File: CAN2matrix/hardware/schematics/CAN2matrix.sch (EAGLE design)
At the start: 31 parts, among them IC1 MEGA8-P, IC2 MCP2515-E/P, IC3 MCP2515-E/P, U1 MCP2551P, U2 MCP2551P, X1 CAN1, X2 CAN2

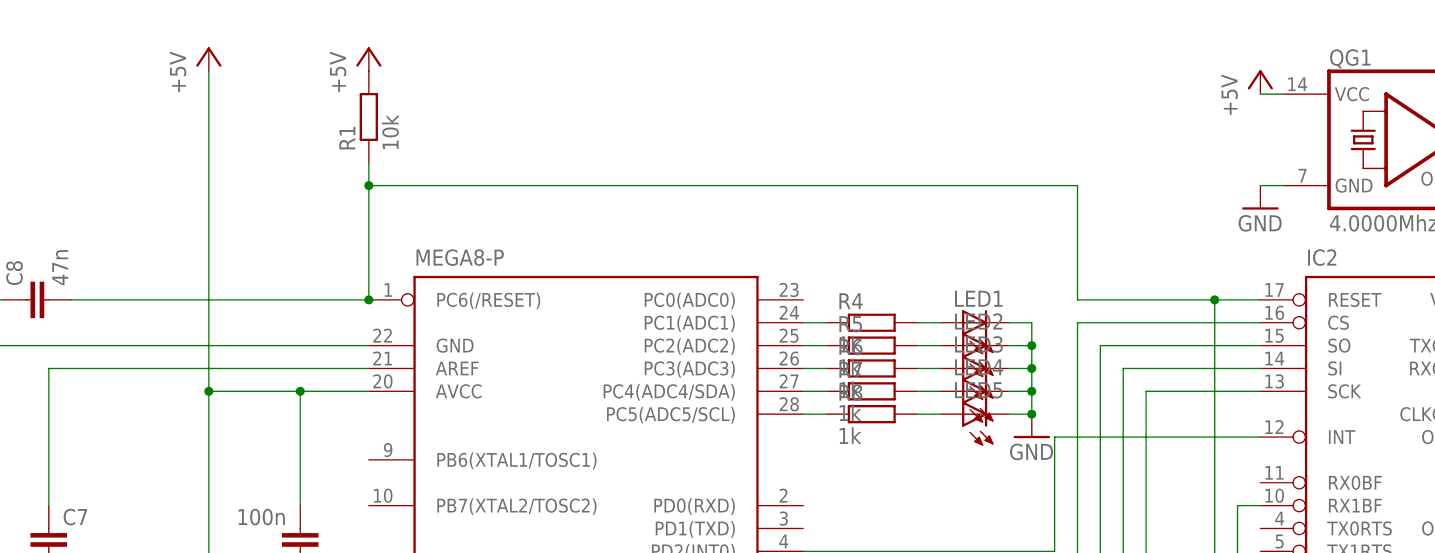
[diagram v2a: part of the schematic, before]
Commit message: add light dependent resistor for dimming; update schematics and image
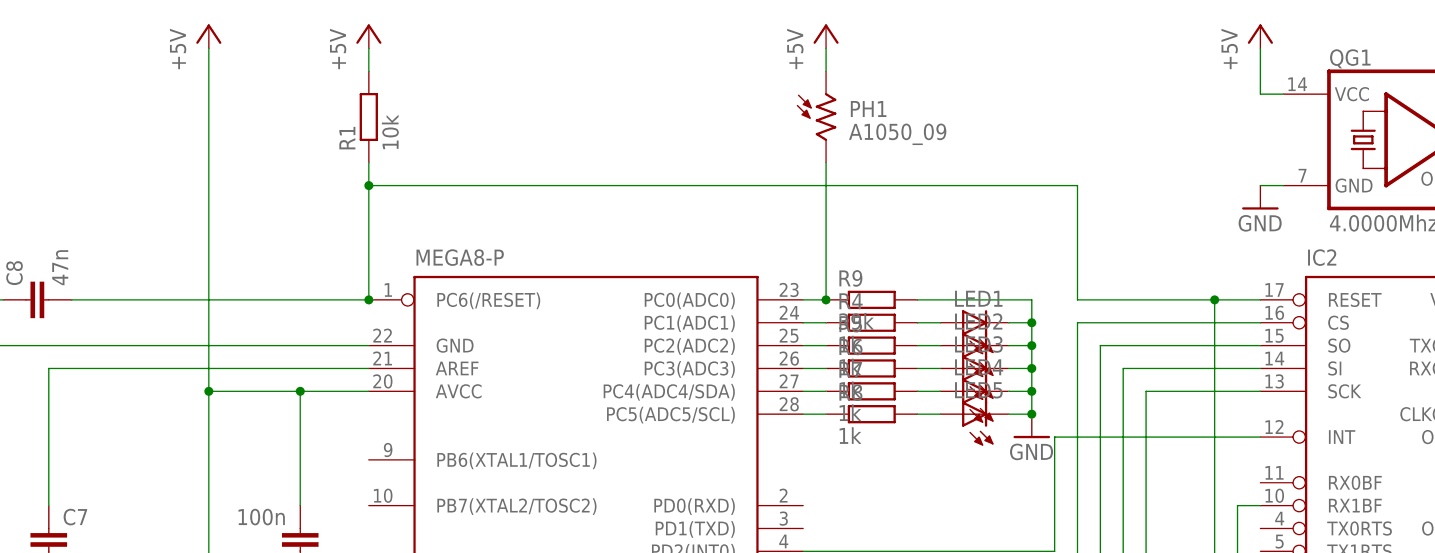
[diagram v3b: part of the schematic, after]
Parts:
- added PH1: A1050_09, photo-elements:A1050_09
- added R9: 39k, resistor:R-EU_0207/2V
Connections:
- new net N$32: IC1.PC0(ADC0), PH1.2, R9.1
- net +5V: now also PH1.1
- net GND: now also R9.2
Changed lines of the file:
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@@
 <grid distance="0.1" unitdist="inch" unit="inch" style="lines" multiple="1" display="no" altdistance="0.01" altunitdist="inch" altunit="inch"/>
 <layers>
-<layer number="1" name="Top" color="4" fill="1" visible="yes" active="no"/>
-<layer number="16" name="Bottom" color="1" fill="1" visible="yes" active="no"/>
-<layer number="17" name="Pads" color="2" fill="1" visible="yes" active="no"/>
-<layer number="18" name="Vias" color="2" fill="1" visible="yes" active="no"/>
-<layer number="19" name="Unrouted" color="6" fill="1" visible="yes" active="no"/>
-<layer number="20" name="Dimension" color="15" fill="1" visible="yes" active="no"/>
-<layer number="21" name="tPlace" color="7" fill="1" visible="yes" active="no"/>
-<layer number="22" name="bPlace" color="7" fill="1" visible="yes" active="no"/>
-<layer number="23" name="tOrigins" color="15" fill="1" visible="yes" active="no"/>
-<layer number="24" name="bOrigins" color="15" fill="1" visible="yes" active="no"/>
-<layer number="25" name="tNames" color="7" fill="1" visible="yes" active="no"/>
-<layer number="26" name="bNames" color="7" fill="1" visible="yes" active="no"/>
-<layer number="27" name="tValues" color="7" fill="1" visible="yes" active="no"/>
-<layer number="28" name="bValues" color="7" fill="1" visible="yes" active="no"/>
+<layer number="1" name="Top" color="4" fill="1" visible="no" active="no"/>
+<layer number="16" name="Bottom" color="1" fill="1" visible="no" active="no"/>
+<layer number="17" name="Pads" color="2" fill="1" visible="no" active="no"/>
+<layer number="18" name="Vias" color="2" fill="1" visible="no" active="no"/>
+<layer number="19" name="Unrouted" color="6" fill="1" visible="no" active="no"/>
+<layer number="20" name="Dimension" color="15" fill="1" visible="no" active="no"/>
+<layer number="21" name="tPlace" color="7" fill="1" visible="no" active="no"/>
+<layer number="22" name="bPlace" color="7" fill="1" visible="no" active="no"/>
+<layer number="23" name="tOrigins" color="15" fill="1" visible="no" active="no"/>
+<layer number="24" name="bOrigins" color="15" fill="1" visible="no" active="no"/>
+<layer number="25" name="tNames" color="7" fill="1" visible="no" active="no"/>
+<layer number="26" name="bNames" color="7" fill="1" visible="no" active="no"/>
+<layer number="27" name="tValues" color="7" fill="1" visible="no" active="no"/>
+<layer number="28" name="bValues" color="7" fill="1" visible="no" active="no"/>
 <layer number="29" name="tStop" color="7" fill="3" visible="no" active="no"/>
 <layer number="30" name="bStop" color="7" fill="6" visible="no" active="no"/>
@@
 <layer number="35" name="tGlue" color="7" fill="4" visible="no" active="no"/>
 <layer number="36" name="bGlue" color="7" fill="5" visible="no" active="no"/>
-<layer number="37" name="tTest" color="7" fill="1" visible="yes" active="no"/>
-<layer number="38" name="bTest" color="7" fill="1" visible="yes" active="no"/>
+<layer number="37" name="tTest" color="7" fill="1" visible="no" active="no"/>
+<layer number="38" name="bTest" color="7" fill="1" visible="no" active="no"/>
 <layer number="39" name="tKeepout" color="4" fill="11" visible="no" active="no"/>
 <layer number="40" name="bKeepout" color="1" fill="11" visible="no" active="no"/>
@@
 <layer number="44" name="Drills" color="7" fill="1" visible="no" active="no"/>
 <layer number="45" name="Holes" color="7" fill="1" visible="no" active="no"/>
-<layer number="46" name="Milling" color="3" fill="1" visible="yes" active="no"/>
-<layer number="47" name="Measures" color="7" fill="1" visible="yes" active="no"/>
-<layer number="48" name="Document" color="7" fill="1" visible="yes" active="no"/>
-<layer number="49" name="Reference" color="7" fill="1" visible="yes" active="no"/>
-<layer number="51" name="tDocu" color="6" fill="9" visible="yes" active="no"/>
-<layer number="52" name="bDocu" color="7" fill="1" visible="yes" active="no"/>
+<layer number="46" name="Milling" color="3" fill="1" visible="no" active="no"/>
+<layer number="47" name="Measures" color="7" fill="1" visible="no" active="no"/>
+<layer number="48" name="Document" color="7" fill="1" visible="no" active="no"/>
+<layer number="49" name="Reference" color="7" fill="1" visible="no" active="no"/>
+<layer number="51" name="tDocu" color="6" fill="9" visible="no" active="no"/>
+<layer number="52" name="bDocu" color="7" fill="1" visible="no" active="no"/>
 <layer number="91" name="Nets" color="2" fill="1" visible="yes" active="yes"/>
 <layer number="92" name="Busses" color="1" fill="1" visible="yes" active="yes"/>
@@
 <part name="LED5" library="led" deviceset="LED" device="3MM"/>
 <part name="GND11" library="supply1" deviceset="GND" device=""/>
+<part name="R9" library="resistor" deviceset="R-EU_" device="0207/2V" value="39k"/>
+<part name="PH1" library="photo-elements" deviceset="A10" device="" technology="50_09"/>
+<part name="P+5" library="supply1" deviceset="+5V" device=""/>
 </parts>
 <sheets>
@@
 <instance part="R2" gate="G$1" x="111.76" y="25.4" rot="R90"/>
 <instance part="R3" gate="G$1" x="111.76" y="-40.64" rot="R90"/>
-<instance part="P+1" gate="1" x="-78.74" y="66.04"/>
+<instance part="P+1" gate="1" x="-78.74" y="68.58"/>
 <instance part="GND1" gate="1" x="-144.78" y="-81.28"/>
-<instance part="P+2" gate="1" x="-96.52" y="66.04"/>
+<instance part="P+2" gate="1" x="-96.52" y="68.58"/>
 <instance part="P+3" gate="1" x="53.34" y="48.26"/>
 <instance part="P+4" gate="1" x="50.8" y="-17.78"/>
@@
 <instance part="C8" gate="G$1" x="-116.84" y="38.1" rot="R90"/>
 <instance part="QG1" gate="G$1" x="35.56" y="55.88"/>
-<instance part="P+10" gate="1" x="20.32" y="63.5"/>
+<instance part="P+10" gate="1" x="20.32" y="68.58"/>
 <instance part="GND8" gate="1" x="20.32" y="48.26"/>
 <instance part="SV1" gate="G$1" x="-17.78" y="-68.58" rot="R180"/>
@@
 <instance part="LED5" gate="G$1" x="-12.7" y="25.4" rot="R90"/>
 <instance part="GND11" gate="1" x="-5.08" y="22.86"/>
+<instance part="R9" gate="G$1" x="-22.86" y="38.1"/>
+<instance part="PH1" gate="G$1" x="-27.94" y="58.42"/>
+<instance part="P+5" gate="1" x="-27.94" y="68.58"/>
 </instances>
 <busses>
@@
 <pinref part="R1" gate="G$1" pin="2"/>
 <pinref part="P+1" gate="1" pin="+5V"/>
+<wire x1="-78.74" y1="66.04" x2="-78.74" y2="63.5" width="0.1524" layer="91"/>
 </segment>
 <segment>
@@
 <segment>
 <pinref part="P+2" gate="1" pin="+5V"/>
-<wire x1="-96.52" y1="63.5" x2="-96.52" y2="27.94" width="0.1524" layer="91"/>
+<wire x1="-96.52" y1="66.04" x2="-96.52" y2="27.94" width="0.1524" layer="91"/>
 <pinref part="IC1" gate="G$1" pin="VCC@1"/>
 <wire x1="-96.52" y1="27.94" x2="-96.52" y2="2.54" width="0.1524" layer="91"/>
@@
 </segment>
 <segment>
-<pinref part="QG1" gate="G$1" pin="VCC"/>
-<pinref part="P+10" gate="1" pin="+5V"/>
-<wire x1="20.32" y1="60.96" x2="22.86" y2="60.96" width="0.1524" layer="91"/>
-</segment>
-<segment>
 <pinref part="IC2" gate="G$1" pin="VDD"/>
 <pinref part="P+3" gate="1" pin="+5V"/>
@@
 <pinref part="SV2" gate="G$1" pin="1"/>
 <wire x1="-10.16" y1="-50.8" x2="-7.62" y2="-50.8" width="0.1524" layer="91"/>
+</segment>
+<segment>
+<pinref part="P+10" gate="1" pin="+5V"/>
+<wire x1="20.32" y1="66.04" x2="20.32" y2="60.96" width="0.1524" layer="91"/>
+<pinref part="QG1" gate="G$1" pin="VCC"/>
+<wire x1="20.32" y1="60.96" x2="22.86" y2="60.96" width="0.1524" layer="91"/>
+</segment>
+<segment>
+<pinref part="P+5" gate="1" pin="+5V"/>
+<pinref part="PH1" gate="G$1" pin="1"/>
+<wire x1="-27.94" y1="66.04" x2="-27.94" y2="63.5" width="0.1524" layer="91"/>
 </segment>
 </net>
@@
 <junction x="-5.08" y="27.94"/>
 <junction x="-5.08" y="25.4"/>
+<pinref part="R9" gate="G$1" pin="2"/>
+<wire x1="-17.78" y1="38.1" x2="-5.08" y2="38.1" width="0.1524" layer="91"/>
+<wire x1="-5.08" y1="38.1" x2="-5.08" y2="35.56" width="0.1524" layer="91"/>
+<junction x="-5.08" y="35.56"/>
 </segment>
 </net>
@@
 </segment>
 </net>
+<net name="N$32" class="0">
+<segment>
+<pinref part="IC1" gate="G$1" pin="PC0(ADC0)"/>
+<pinref part="R9" gate="G$1" pin="1"/>
+<wire x1="-30.48" y1="38.1" x2="-27.94" y2="38.1" width="0.1524" layer="91"/>
+<pinref part="PH1" gate="G$1" pin="2"/>
+<wire x1="-27.94" y1="53.34" x2="-27.94" y2="38.1" width="0.1524" layer="91"/>
+<junction x="-27.94" y="38.1"/>
+</segment>
+</net>

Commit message: add first pcb (placement only) to hardware (Eagle 6.1.0)
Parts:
- LED1, LED2: value (none) -> red
- LED3, LED4: value (none) -> green
- LED5: value (none) -> yellow
- R1, R2, R3: device resistor:R-EU_0207/12 -> resistor:R-EU_0207/2V
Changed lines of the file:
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@@
 <grid distance="0.1" unitdist="inch" unit="inch" style="lines" multiple="1" display="no" altdistance="0.01" altunitdist="inch" altunit="inch"/>
 <layers>
-<layer number="1" name="Top" color="4" fill="1" visible="no" active="no"/>
-<layer number="16" name="Bottom" color="1" fill="1" visible="no" active="no"/>
-<layer number="17" name="Pads" color="2" fill="1" visible="no" active="no"/>
-<layer number="18" name="Vias" color="2" fill="1" visible="no" active="no"/>
-<layer number="19" name="Unrouted" color="6" fill="1" visible="no" active="no"/>
-<layer number="20" name="Dimension" color="15" fill="1" visible="no" active="no"/>
-<layer number="21" name="tPlace" color="7" fill="1" visible="no" active="no"/>
-<layer number="22" name="bPlace" color="7" fill="1" visible="no" active="no"/>
-<layer number="23" name="tOrigins" color="15" fill="1" visible="no" active="no"/>
-<layer number="24" name="bOrigins" color="15" fill="1" visible="no" active="no"/>
-<layer number="25" name="tNames" color="7" fill="1" visible="no" active="no"/>
-<layer number="26" name="bNames" color="7" fill="1" visible="no" active="no"/>
-<layer number="27" name="tValues" color="7" fill="1" visible="no" active="no"/>
-<layer number="28" name="bValues" color="7" fill="1" visible="no" active="no"/>
+<layer number="1" name="Top" color="4" fill="1" visible="yes" active="no"/>
+<layer number="16" name="Bottom" color="1" fill="1" visible="yes" active="no"/>
+<layer number="17" name="Pads" color="2" fill="1" visible="yes" active="no"/>
+<layer number="18" name="Vias" color="2" fill="1" visible="yes" active="no"/>
+<layer number="19" name="Unrouted" color="6" fill="1" visible="yes" active="no"/>
+<layer number="20" name="Dimension" color="15" fill="1" visible="yes" active="no"/>
+<layer number="21" name="tPlace" color="7" fill="1" visible="yes" active="no"/>
+<layer number="22" name="bPlace" color="7" fill="1" visible="yes" active="no"/>
+<layer number="23" name="tOrigins" color="15" fill="1" visible="yes" active="no"/>
+<layer number="24" name="bOrigins" color="15" fill="1" visible="yes" active="no"/>
+<layer number="25" name="tNames" color="7" fill="1" visible="yes" active="no"/>
+<layer number="26" name="bNames" color="7" fill="1" visible="yes" active="no"/>
+<layer number="27" name="tValues" color="7" fill="1" visible="yes" active="no"/>
+<layer number="28" name="bValues" color="7" fill="1" visible="yes" active="no"/>
 <layer number="29" name="tStop" color="7" fill="3" visible="no" active="no"/>
 <layer number="30" name="bStop" color="7" fill="6" visible="no" active="no"/>
@@
 <layer number="35" name="tGlue" color="7" fill="4" visible="no" active="no"/>
 <layer number="36" name="bGlue" color="7" fill="5" visible="no" active="no"/>
-<layer number="37" name="tTest" color="7" fill="1" visible="no" active="no"/>
-<layer number="38" name="bTest" color="7" fill="1" visible="no" active="no"/>
+<layer number="37" name="tTest" color="7" fill="1" visible="yes" active="no"/>
+<layer number="38" name="bTest" color="7" fill="1" visible="yes" active="no"/>
 <layer number="39" name="tKeepout" color="4" fill="11" visible="no" active="no"/>
 <layer number="40" name="bKeepout" color="1" fill="11" visible="no" active="no"/>
@@
 <layer number="44" name="Drills" color="7" fill="1" visible="no" active="no"/>
 <layer number="45" name="Holes" color="7" fill="1" visible="no" active="no"/>
-<layer number="46" name="Milling" color="3" fill="1" visible="no" active="no"/>
-<layer number="47" name="Measures" color="7" fill="1" visible="no" active="no"/>
-<layer number="48" name="Document" color="7" fill="1" visible="no" active="no"/>
-<layer number="49" name="Reference" color="7" fill="1" visible="no" active="no"/>
-<layer number="51" name="tDocu" color="6" fill="9" visible="no" active="no"/>
-<layer number="52" name="bDocu" color="7" fill="1" visible="no" active="no"/>
+<layer number="46" name="Milling" color="3" fill="1" visible="yes" active="no"/>
+<layer number="47" name="Measures" color="7" fill="1" visible="yes" active="no"/>
+<layer number="48" name="Document" color="7" fill="1" visible="yes" active="no"/>
+<layer number="49" name="Reference" color="7" fill="1" visible="yes" active="no"/>
+<layer number="51" name="tDocu" color="7" fill="1" visible="yes" active="no"/>
+<layer number="52" name="bDocu" color="7" fill="1" visible="yes" active="no"/>
 <layer number="91" name="Nets" color="2" fill="1" visible="yes" active="yes"/>
 <layer number="92" name="Busses" color="1" fill="1" visible="yes" active="yes"/>
@@
 <part name="IC2" library="mcp2515" deviceset="MCP2515" device="-E/P"/>
 <part name="IC3" library="mcp2515" deviceset="MCP2515" device="-E/P"/>
-<part name="R1" library="resistor" deviceset="R-EU_" device="0207/12" value="10k"/>
-<part name="R2" library="resistor" deviceset="R-EU_" device="0207/12" value="120"/>
-<part name="R3" library="resistor" deviceset="R-EU_" device="0207/12" value="120"/>
+<part name="R1" library="resistor" deviceset="R-EU_" device="0207/2V" value="10k"/>
+<part name="R2" library="resistor" deviceset="R-EU_" device="0207/2V" value="120"/>
+<part name="R3" library="resistor" deviceset="R-EU_" device="0207/2V" value="120"/>
 <part name="P+1" library="supply1" deviceset="+5V" device=""/>
 <part name="GND1" library="supply1" deviceset="GND" device=""/>
@@
 <part name="R7" library="resistor" deviceset="R-EU_" device="0207/2V" value="1k"/>
 <part name="R8" library="resistor" deviceset="R-EU_" device="0207/2V" value="1k"/>
-<part name="LED1" library="led" deviceset="LED" device="3MM"/>
-<part name="LED2" library="led" deviceset="LED" device="3MM"/>
-<part name="LED3" library="led" deviceset="LED" device="3MM"/>
-<part name="LED4" library="led" deviceset="LED" device="3MM"/>
-<part name="LED5" library="led" deviceset="LED" device="3MM"/>
+<part name="LED1" library="led" deviceset="LED" device="3MM" value="red"/>
+<part name="LED2" library="led" deviceset="LED" device="3MM" value="red"/>
+<part name="LED3" library="led" deviceset="LED" device="3MM" value="green"/>
+<part name="LED4" library="led" deviceset="LED" device="3MM" value="green"/>
+<part name="LED5" library="led" deviceset="LED" device="3MM" value="yellow"/>
 <part name="GND11" library="supply1" deviceset="GND" device=""/>
 <part name="R9" library="resistor" deviceset="R-EU_" device="0207/2V" value="39k"/>
@@
 <pinref part="U2" gate="P" pin="VDD"/>
 <wire x1="-93.98" y1="-63.5" x2="-101.6" y2="-63.5" width="0.1524" layer="91"/>
+<junction x="-101.6" y="-63.5"/>
 </segment>
 <segment>
@@
 <pinref part="U1" gate="P" pin="VDD"/>
 <wire x1="-73.66" y1="-63.5" x2="-81.28" y2="-63.5" width="0.1524" layer="91"/>
+<junction x="-81.28" y="-63.5"/>
 </segment>
 <segment>
@@
 <pinref part="U2" gate="P" pin="VSS"/>
 <wire x1="-93.98" y1="-78.74" x2="-101.6" y2="-78.74" width="0.1524" layer="91"/>
+<junction x="-101.6" y="-78.74"/>
 </segment>
 <segment>
@@
 <pinref part="U1" gate="P" pin="VSS"/>
 <wire x1="-73.66" y1="-78.74" x2="-81.28" y2="-78.74" width="0.1524" layer="91"/>
+<junction x="-81.28" y="-78.74"/>
 </segment>
 <segment>
@@
 </sheet>
 </sheets>
+<errors>
+</errors>
 </schematic>
 </drawing>

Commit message: V1.0 of PCB and adjusted schematics
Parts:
- R4, R5, R6, R7, R8: device resistor:R-EU_0207/2V -> resistor:R-EU_0207/10
- R9: device resistor:R-EU_0207/2V -> resistor:R-EU_0204/7
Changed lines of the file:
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@@
 <part name="GND3" library="supply1" deviceset="GND" device=""/>
 <part name="SV2" library="con-lstb" deviceset="MA03-1" device="" value="Ext Pwr"/>
-<part name="R4" library="resistor" deviceset="R-EU_" device="0207/2V" value="1k"/>
-<part name="R5" library="resistor" deviceset="R-EU_" device="0207/2V" value="1k"/>
-<part name="R6" library="resistor" deviceset="R-EU_" device="0207/2V" value="1k"/>
-<part name="R7" library="resistor" deviceset="R-EU_" device="0207/2V" value="1k"/>
-<part name="R8" library="resistor" deviceset="R-EU_" device="0207/2V" value="1k"/>
+<part name="R4" library="resistor" deviceset="R-EU_" device="0207/10" value="1k"/>
+<part name="R5" library="resistor" deviceset="R-EU_" device="0207/10" value="1k"/>
+<part name="R6" library="resistor" deviceset="R-EU_" device="0207/10" value="1k"/>
+<part name="R7" library="resistor" deviceset="R-EU_" device="0207/10" value="1k"/>
+<part name="R8" library="resistor" deviceset="R-EU_" device="0207/10" value="1k"/>
 <part name="LED1" library="led" deviceset="LED" device="3MM" value="red"/>
 <part name="LED2" library="led" deviceset="LED" device="3MM" value="red"/>
@@
 <part name="LED5" library="led" deviceset="LED" device="3MM" value="yellow"/>
 <part name="GND11" library="supply1" deviceset="GND" device=""/>
-<part name="R9" library="resistor" deviceset="R-EU_" device="0207/2V" value="39k"/>
+<part name="R9" library="resistor" deviceset="R-EU_" device="0204/7" value="39k"/>
 <part name="PH1" library="photo-elements" deviceset="A10" device="" technology="50_09"/>
 <part name="P+5" library="supply1" deviceset="+5V" device=""/>
@@
 <wire x1="-30.48" y1="-15.24" x2="5.08" y2="-15.24" width="0.1524" layer="91"/>
 <junction x="5.08" y="-15.24"/>
-<pinref part="SV1" gate="G$1" pin="1"/>
 <wire x1="5.08" y1="-35.56" x2="-30.48" y2="-35.56" width="0.1524" layer="91"/>
 <wire x1="-30.48" y1="-35.56" x2="-30.48" y2="-63.5" width="0.1524" layer="91"/>
-<wire x1="-30.48" y1="-63.5" x2="-25.4" y2="-63.5" width="0.1524" layer="91"/>
 <junction x="5.08" y="-35.56"/>
+<pinref part="SV1" gate="G$1" pin="1"/>
+<wire x1="-25.4" y1="-63.5" x2="-30.48" y2="-63.5" width="0.1524" layer="91"/>
 </segment>
 </net>

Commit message: add non-USB power supply to schematics and PCB; export images
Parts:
- added C10: 100n, resistor:C-EU050-025X075
- added C11: 1µ, resistor:CPOL-EUE2.5-7
- added C9: 330n, resistor:C-EU050-025X075
- added D1: 1N4002, diode:1N4004
- added IC4: (no value), v-reg:78LXX
- added LSP1: +12V, solpad:SE14
- added LSP2: SE14, solpad:SE14
- added SV3: Ext Pwr, con-lstb:MA03-1
- SV2: value Ext Pwr -> USB Pwr
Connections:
- new net +12V: C9.1, D1.C, IC4.IN, LSP1.MP
- new net N$33: C10.1, C11.+, D1.A, IC4.OUT, SV3.3
- net +5V: now also SV3.2
- net GND: now also C10.2, C11.-, C9.2, IC4.GND, LSP2.MP
